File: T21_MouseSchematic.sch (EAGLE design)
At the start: 26 parts, among them IC1 L293D, U2 LD1086D2XX, U3 V_REG_LD1085D2

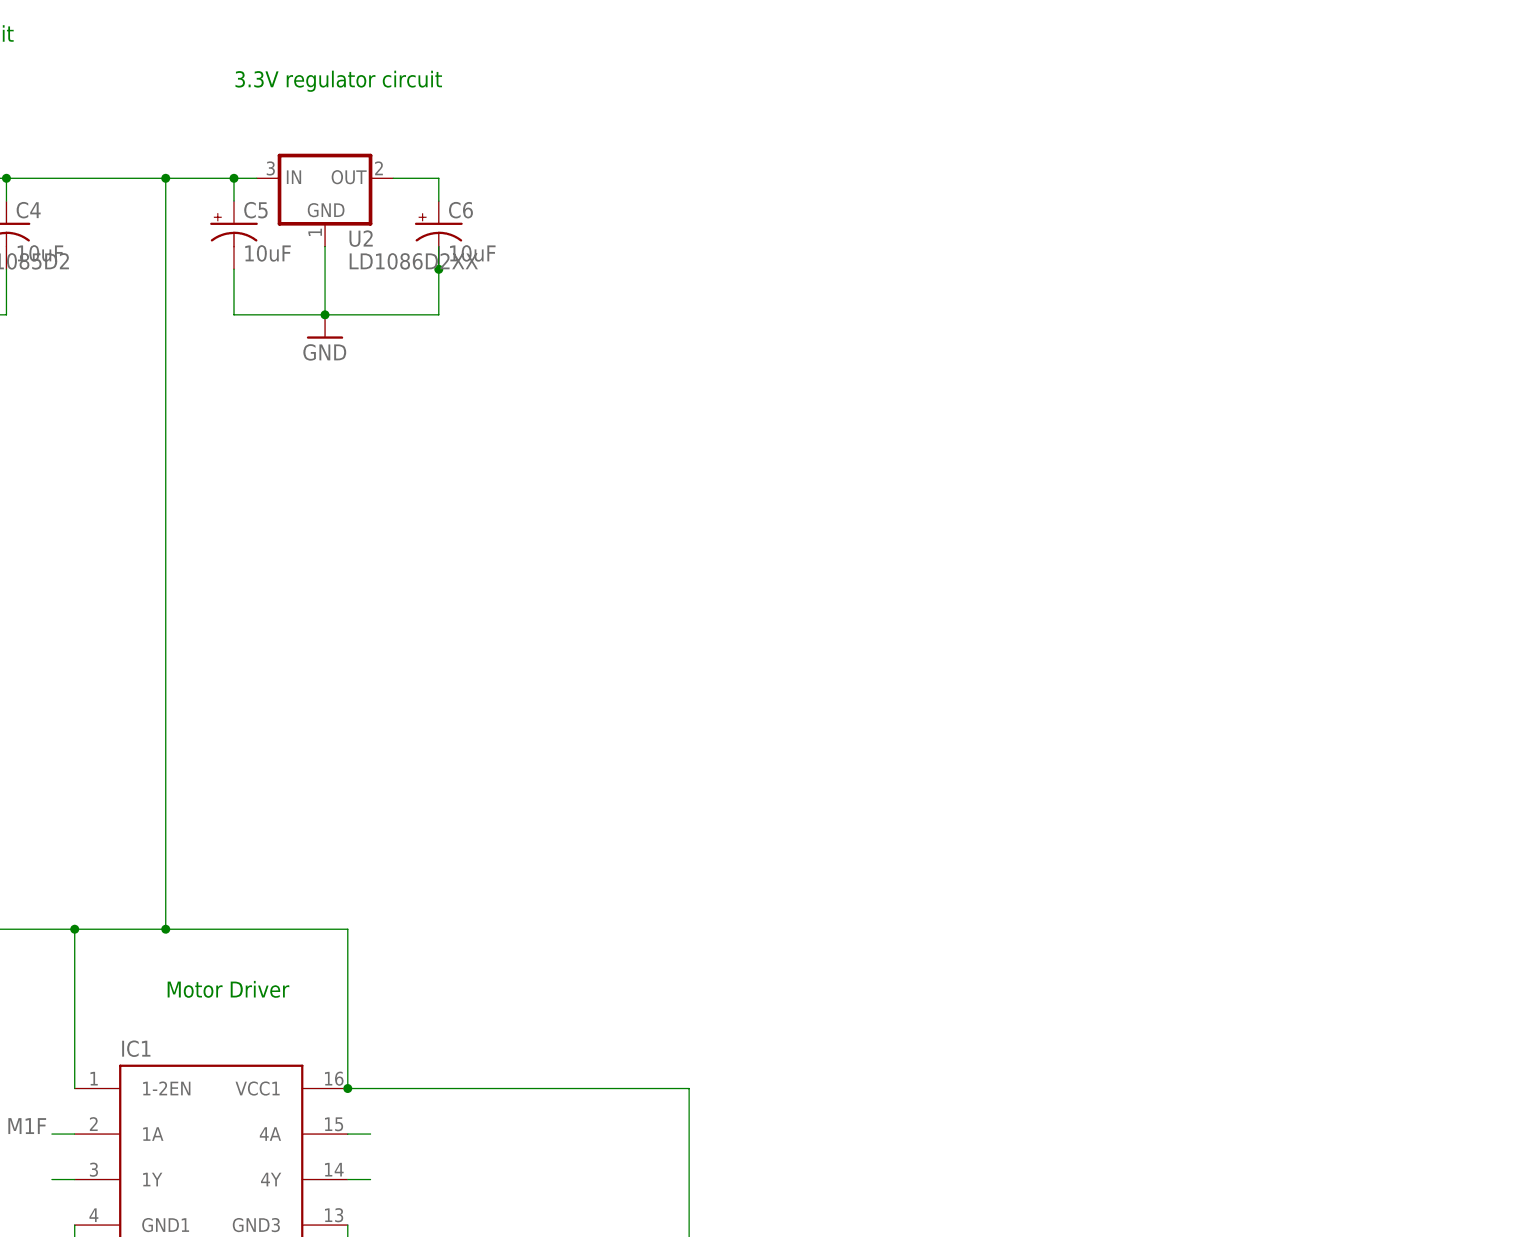
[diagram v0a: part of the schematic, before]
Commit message: Update Schematic
Added IMU and distance sensors
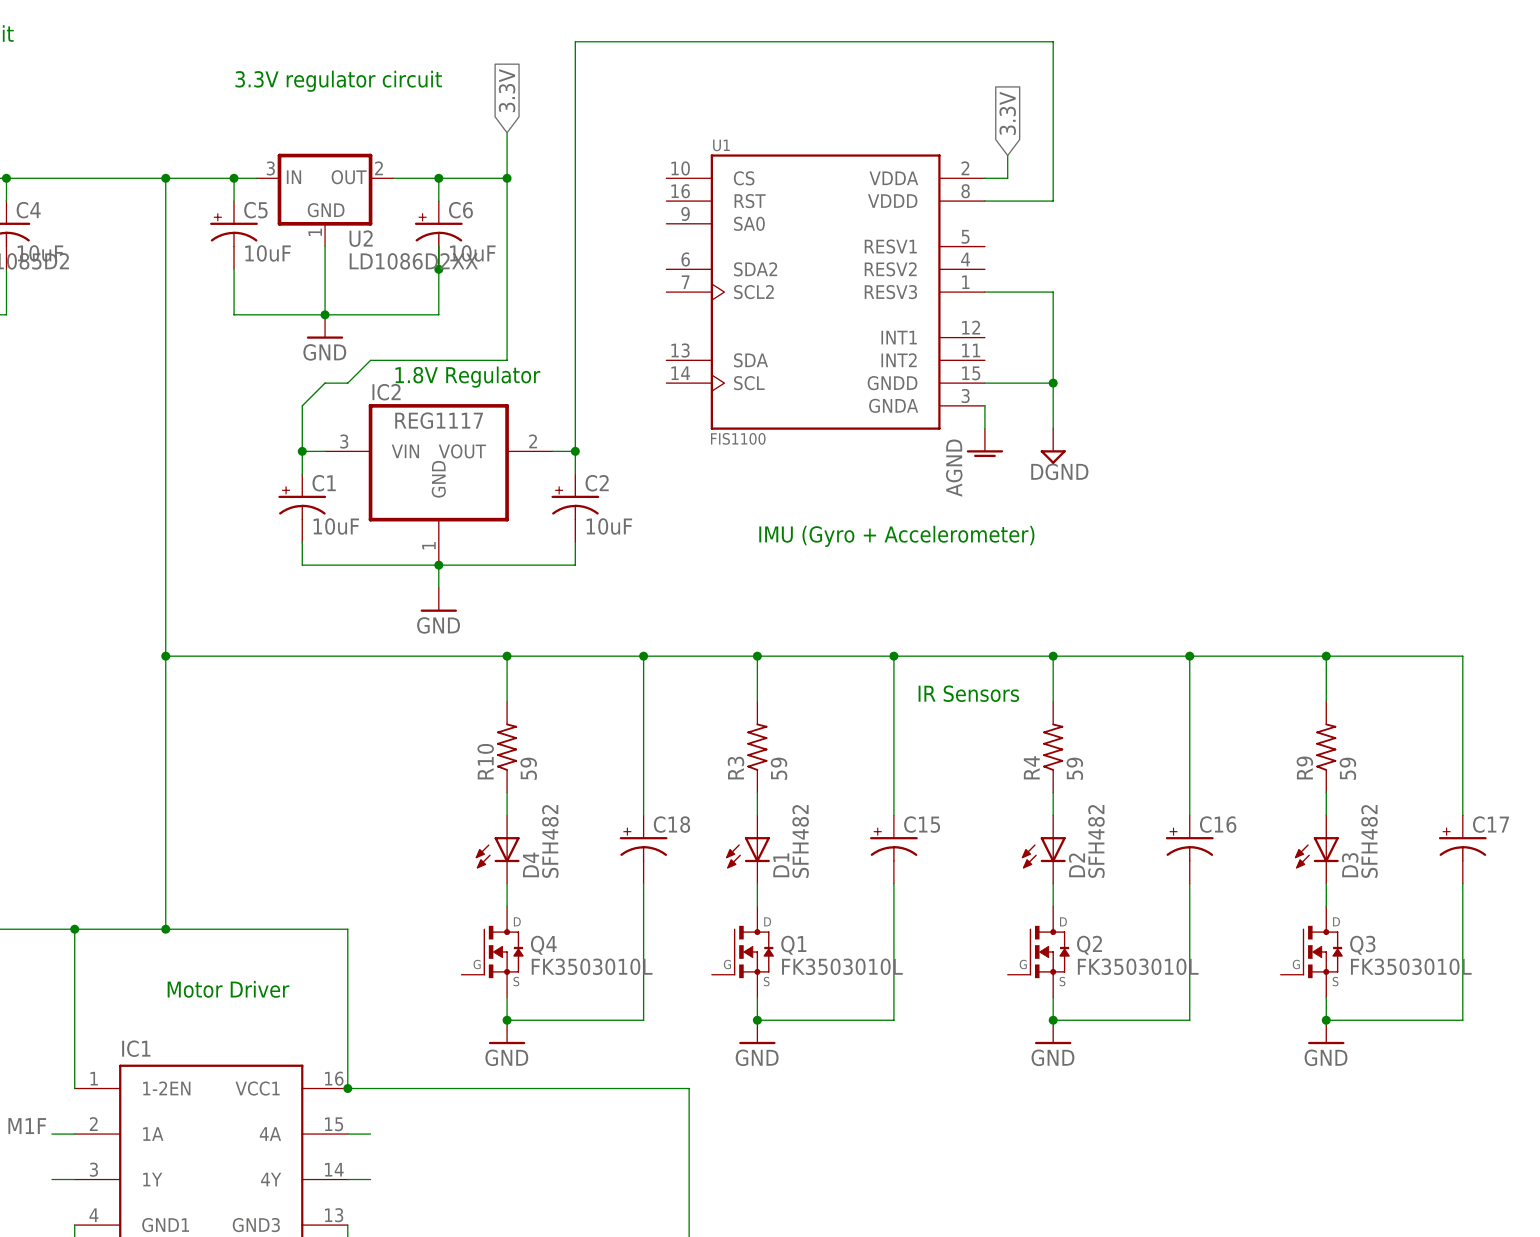
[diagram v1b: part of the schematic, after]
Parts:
- added C1, C2: 10uF, SparkFun:CAP_POLE
- added C15, C16, C17, C18: (no value), SparkFun:CAP_POLE
- added D1, D2, D3, D4: SFH482, led:SFH482
- added IC2: REG1117, burr-brown:REG1117
- added Q1, Q2, Q3, Q4: FK3503010L, transistor-fet:FK3503010L
- added R10, R3, R4, R9: 59, rcl:R-US_R0603
- added U1: FIS1100, FIS1100:FIS1100
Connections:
- new net 3.3V: C1.+, C6.+, IC2.VIN, U1.VDDA, U2.OUT
- new net DGND: U1.GNDD, U1.RESV3
- new net N$25: D4.C, Q4.D
- new net N$26: D4.A, R10.1
- new net N$3: D1.C, Q1.D
- new net N$4: C2.+, IC2.VOUT, U1.VDDD
- new net N$5: D1.A, R3.1
- new net N$7: D2.C, Q2.D
- new net N$8: D2.A, R4.1
- new net N$9: D3.C, Q3.D
- net 5V: now also C15.+, C16.+, C17.+, C18.+, R10.2, R3.2, R4.2, R9.2
- net AGND: now also U1.GNDA
- net GND: now also C1.-, C15.-, C16.-, C17.-, C18.-, C2.-, IC2.GND, Q1.S, Q2.S, Q3.S, Q4.S
- net N$11: now also D3.A, R9.1; no longer C6.+, U2.OUT
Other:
- note added: "1.8V Regulator"
- note added: "IMU (Gyro + Accelerometer)"
- note added: "IR Sensors"
